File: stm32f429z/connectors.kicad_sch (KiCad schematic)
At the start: 18 parts, among them J1 ADC connector 2, J10 UART 1 connectors, J12 USB to UART GPIO, J14 I2C 1 connector, J2 ADC connector 1, J3 SPI 2 connector, J4 SPI 1 connector, J5 I2C 2 connector, J8 SWD

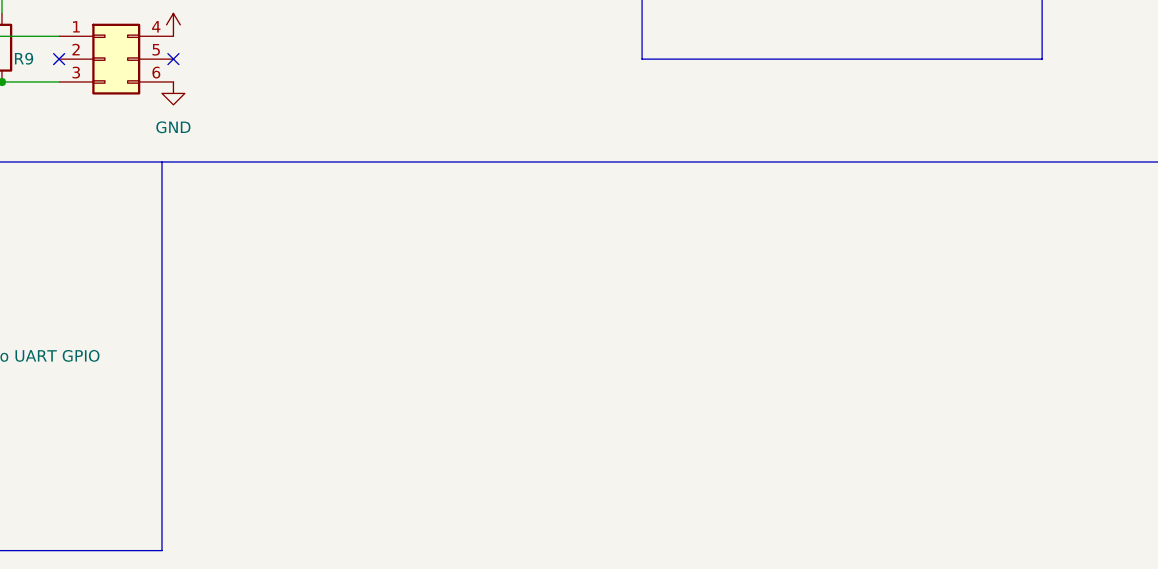
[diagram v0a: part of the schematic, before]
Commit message: removed alot of the silk screen, changed oscillator foor print and added GPIOs
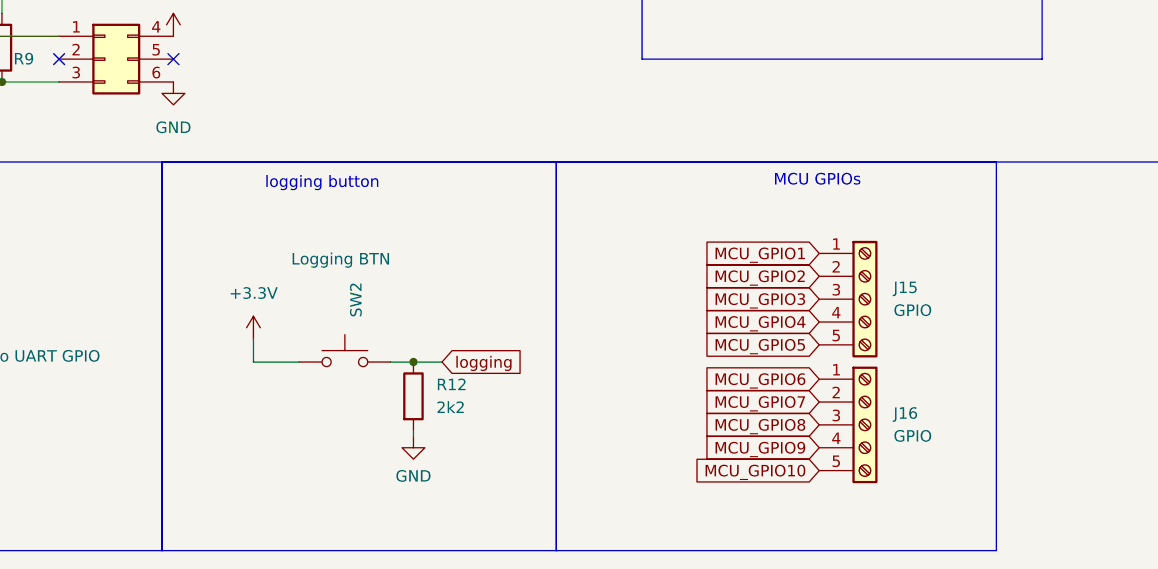
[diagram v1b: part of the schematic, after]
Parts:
- added J15, J16: GPIO, TerminalBlock_Phoenix:TerminalBlock_Phoenix_MKDS-1,5-5_1x05_P5.00mm_Horizontal, symbol Connector:Screw_Terminal_01x05
- added R12: 2k2, Resistor_SMD:R_0603_1608Metric_Pad0.98x0.95mm_HandSolder, symbol Device:R
- added SW2: Logging BTN, Button_Switch_SMD:SW_SPST_PTS645, symbol Switch:SW_Push
- J8: footprint Connector_PinHeader_2.54mm:PinHeader_2x05_P2.54mm_Vertical_SMD -> Connector_PinHeader_2.54mm:PinHeader_2x05_P2.54mm_Vertical
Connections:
- net +3.3V: now also SW2.1
- net GND: now also R12.2
- new net MCU_GPIO1: J15.1 (Pin_1)
- new net MCU_GPIO10: J16.5 (Pin_5)
- new net MCU_GPIO2: J15.2 (Pin_2)
- new net MCU_GPIO3: J15.3 (Pin_3)
- new net MCU_GPIO4: J15.4 (Pin_4)
- new net MCU_GPIO5: J15.5 (Pin_5)
- new net MCU_GPIO6: J16.1 (Pin_1)
- new net MCU_GPIO7: J16.2 (Pin_2)
- new net MCU_GPIO8: J16.3 (Pin_3)
- new net MCU_GPIO9: J16.4 (Pin_4)
- new net logging: R12.1, SW2.2
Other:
- note added: "MCU GPIOs"
- note added: "logging button"

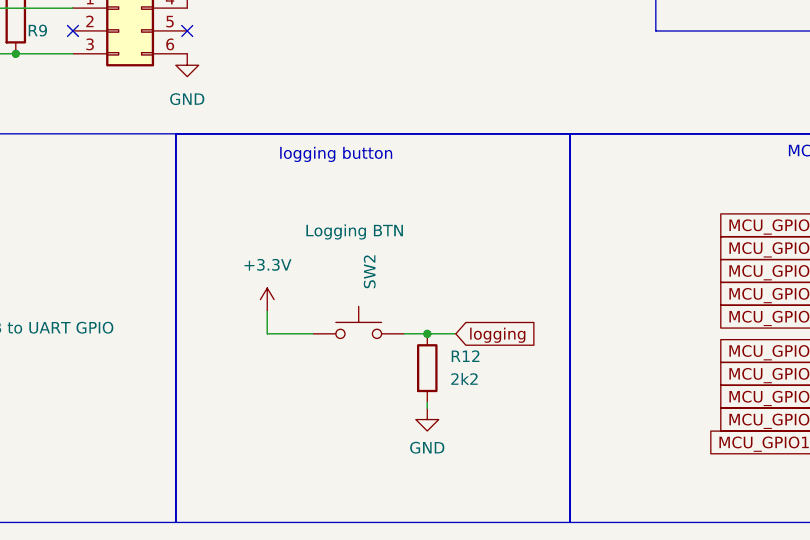
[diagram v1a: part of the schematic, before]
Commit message: changed logging schematic, tweaked some parts of the schematic
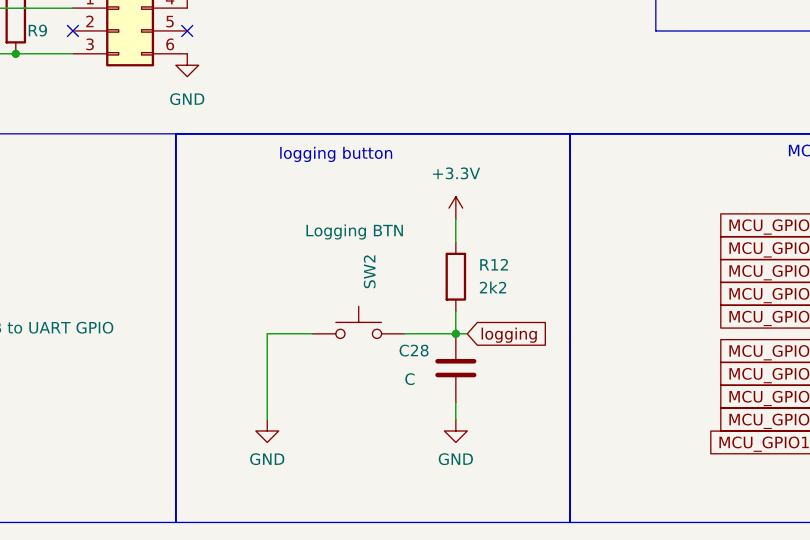
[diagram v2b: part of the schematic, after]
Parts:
- added C28: C, Capacitor_SMD:C_0603_1608Metric_Pad1.08x0.95mm_HandSolder, symbol Device:C
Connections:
- net +3.3V: now also R12.1; no longer SW2.1
- net GND: now also SW2.1, C28.2; no longer R12.2
- net logging: now also R12.2, C28.1; no longer R12.1
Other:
- moved on the sheet: R12
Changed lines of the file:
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@@
   (junction (at 196.85 31.75) (diameter 0) (color 0 0 0 0)
   )
-  (junction (at 177.8 139.065) (diameter 0) (color 0 0 0 0)
-  )
   (junction (at 50.8 88.9) (diameter 0) (color 0 0 0 0)
   )
@@
   )
   (junction (at 203.2 41.91) (diameter 0) (color 0 0 0 0)
+  )
+  (junction (at 180.975 139.065) (diameter 0) (color 0 0 0 0)
   )
   (junction (at 46.99 102.87) (diameter 0) (color 0 0 0 0)
@@
   (no_connect (at 46.99 140.97))
   (no_connect (at 60.96 105.41))
-  (wire (pts (xy 175.26 139.065) (xy 177.8 139.065))
-    (stroke (width 0) (type default))
-  )
   (wire (pts (xy 138.43 107.95) (xy 132.08 107.95))
     (stroke (width 0) (type default))
@@
     (stroke (width 0) (type default))
   )
+  (wire (pts (xy 180.975 148.59) (xy 180.975 146.685))
+    (stroke (width 0) (type default))
+  )
   (wire (pts (xy 196.85 40.64) (xy 196.85 41.91))
     (stroke (width 0) (type default))
@@
     (stroke (width 0) (type default))
   )
+  (wire (pts (xy 160.02 139.065) (xy 160.02 148.59))
+    (stroke (width 0) (type default))
+  )
   (wire (pts (xy 218.44 34.29) (xy 220.98 34.29))
     (stroke (width 0) (type default))
@@
     (stroke (width 0) (type default))
   )
-  (wire (pts (xy 177.8 147.32) (xy 177.8 146.685))
-    (stroke (width 0) (type default))
-  )
   (polyline (pts (xy 187.96 72.39) (xy 284.48 72.39))
     (stroke (width 0) (type default))
@@
     (stroke (width 0) (type default))
   )
-  (wire (pts (xy 177.8 139.065) (xy 180.975 139.065))
+  (wire (pts (xy 175.26 139.065) (xy 180.975 139.065))
     (stroke (width 0) (type default))
   )
@@
     (stroke (width 0) (type default))
   )
+  (wire (pts (xy 180.975 139.065) (xy 182.245 139.065))
+    (stroke (width 0) (type default))
+  )
   (polyline (pts (xy 74.93 24.13) (xy 74.93 72.39))
     (stroke (width 0) (type default))
@@
     (stroke (width 0) (type default))
   )
-  (wire (pts (xy 160.02 139.065) (xy 160.02 136.525))
-    (stroke (width 0) (type default))
-  )
   (wire (pts (xy 132.08 100.33) (xy 132.08 88.9))
     (stroke (width 0) (type default))
@@
     (stroke (width 0) (type default))
   )
+  (wire (pts (xy 180.975 126.365) (xy 180.975 128.905))
+    (stroke (width 0) (type default))
+  )
   (wire (pts (xy 228.6 41.91) (xy 231.14 41.91))
     (stroke (width 0) (type default))
@@
   )
   (wire (pts (xy 60.96 102.87) (xy 46.99 102.87))
+    (stroke (width 0) (type default))
+  )
+  (wire (pts (xy 180.975 136.525) (xy 180.975 139.065))
     (stroke (width 0) (type default))
   )
@@
     )
   )
-  (global_label "logging" (shape input) (at 180.975 139.065 0) (fields_autoplaced)
+  (global_label "logging" (shape input) (at 182.245 139.065 0) (fields_autoplaced)
     (effects (font (size 1.27 1.27)) (justify left))
-    (property "Intersheetrefs" "${INTERSHEET_REFS}" (at 190.9752 139.065 0)
+    (property "Intersheetrefs" "${INTERSHEET_REFS}" (at 192.2452 139.065 0)
       (effects (font (size 1.27 1.27)) (justify left) hide)
     )
@@
     )
   )
-  (symbol (lib_id "Device:R") (at 177.8 142.875 0) (unit 1)
-    (in_bom yes) (on_board yes) (dnp no) (fields_autoplaced)
-    (property "Reference" "R12" (at 180.34 141.605 0)
-      (effects (font (size 1.27 1.27)) (justify left))
-    )
-    (property "Value" "2k2" (at 180.34 144.145 0)
-      (effects (font (size 1.27 1.27)) (justify left))
-    )
-    (property "Footprint" "Resistor_SMD:R_0603_1608Metric_Pad0.98x0.95mm_HandSolder" (at 176.022 142.875 90)
-      (effects (font (size 1.27 1.27)) hide)
-    )
-    (property "Datasheet" "~" (at 177.8 142.875 0)
+  (symbol (lib_id "Device:R") (at 180.975 132.715 0) (unit 1)
+    (in_bom yes) (on_board yes) (dnp no) (fields_autoplaced)
+    (property "Reference" "R12" (at 183.515 131.445 0)
+      (effects (font (size 1.27 1.27)) (justify left))
+    )
+    (property "Value" "2k2" (at 183.515 133.985 0)
+      (effects (font (size 1.27 1.27)) (justify left))
+    )
+    (property "Footprint" "Resistor_SMD:R_0603_1608Metric_Pad0.98x0.95mm_HandSolder" (at 179.197 132.715 90)
+      (effects (font (size 1.27 1.27)) hide)
+    )
+    (property "Datasheet" "~" (at 180.975 132.715 0)
       (effects (font (size 1.27 1.27)) hide)
     )
@@
         (path "/09c21947-d3c4-4f82-9fb4-45f647ba61fc/7392f493-4466-4071-98c2-c2793c4b971d"
           (reference "R12") (unit 1)
+        )
+      )
+    )
+  )
+  (symbol (lib_id "power:GND") (at 180.975 148.59 0) (unit 1)
+    (in_bom yes) (on_board yes) (dnp no) (fields_autoplaced)
+    (property "Reference" "#PWR049" (at 180.975 154.94 0)
+      (effects (font (size 1.27 1.27)) hide)
+    )
+    (property "Value" "GND" (at 180.975 153.035 0)
+      (effects (font (size 1.27 1.27)))
+    )
+    (property "Footprint" "" (at 180.975 148.59 0)
+      (effects (font (size 1.27 1.27)) hide)
+    )
+    (property "Datasheet" "" (at 180.975 148.59 0)
+      (effects (font (size 1.27 1.27)) hide)
+    )
+    (pin "1")
+    (instances
+      (project "stm32f429z"
+        (path "/09c21947-d3c4-4f82-9fb4-45f647ba61fc/7392f493-4466-4071-98c2-c2793c4b971d"
+          (reference "#PWR049") (unit 1)
         )
       )
@@
     )
   )
+  (symbol (lib_id "Device:C") (at 180.975 142.875 0) (unit 1)
+    (in_bom yes) (on_board yes) (dnp no)
+    (property "Reference" "C28" (at 174.625 140.97 0)
+      (effects (font (size 1.27 1.27)) (justify left))
+    )
+    (property "Value" "C" (at 175.26 144.145 0)
+      (effects (font (size 1.27 1.27)) (justify left))
+    )
+    (property "Footprint" "Capacitor_SMD:C_0603_1608Metric_Pad1.08x0.95mm_HandSolder" (at 181.9402 146.685 0)
+      (effects (font (size 1.27 1.27)) hide)
+    )
+    (property "Datasheet" "~" (at 180.975 142.875 0)
+      (effects (font (size 1.27 1.27)) hide)
+    )
+    (pin "1")
+    (pin "2")
+    (instances
+      (project "stm32f429z"
+        (path "/09c21947-d3c4-4f82-9fb4-45f647ba61fc/7392f493-4466-4071-98c2-c2793c4b971d"
+          (reference "C28") (unit 1)
+        )
+      )
+    )
+  )
   (symbol (lib_id "power:+5V") (at 59.69 138.43 0) (unit 1)
     (in_bom yes) (on_board yes) (dnp no) (fields_autoplaced)
@@
     )
   )
-  (symbol (lib_id "power:+3.3V") (at 160.02 136.525 0) (unit 1)
-    (in_bom yes) (on_board yes) (dnp no) (fields_autoplaced)
-    (property "Reference" "#PWR047" (at 160.02 140.335 0)
-      (effects (font (size 1.27 1.27)) hide)
-    )
-    (property "Value" "+3.3V" (at 160.02 131.445 0)
-      (effects (font (size 1.27 1.27)))
-    )
-    (property "Footprint" "" (at 160.02 136.525 0)
-      (effects (font (size 1.27 1.27)) hide)
-    )
-    (property "Datasheet" "" (at 160.02 136.525 0)
-      (effects (font (size 1.27 1.27)) hide)
-    )
-    (pin "1")
-    (instances
-      (project "stm32f429z"
-        (path "/09c21947-d3c4-4f82-9fb4-45f647ba61fc/7392f493-4466-4071-98c2-c2793c4b971d"
-          (reference "#PWR047") (unit 1)
-        )
-      )
-    )
-  )
   (symbol (lib_id "power:+5V") (at 151.13 102.87 0) (unit 1)
     (in_bom yes) (on_board yes) (dnp no) (fields_autoplaced)
@@
     )
   )
-  (symbol (lib_id "power:GND") (at 177.8 147.32 0) (unit 1)
-    (in_bom yes) (on_board yes) (dnp no) (fields_autoplaced)
-    (property "Reference" "#PWR048" (at 177.8 153.67 0)
-      (effects (font (size 1.27 1.27)) hide)
-    )
-    (property "Value" "GND" (at 177.8 151.765 0)
-      (effects (font (size 1.27 1.27)))
-    )
-    (property "Footprint" "" (at 177.8 147.32 0)
-      (effects (font (size 1.27 1.27)) hide)
-    )
-    (property "Datasheet" "" (at 177.8 147.32 0)
+  (symbol (lib_id "power:GND") (at 160.02 148.59 0) (unit 1)
+    (in_bom yes) (on_board yes) (dnp no) (fields_autoplaced)
+    (property "Reference" "#PWR048" (at 160.02 154.94 0)
+      (effects (font (size 1.27 1.27)) hide)
+    )
+    (property "Value" "GND" (at 160.02 153.035 0)
+      (effects (font (size 1.27 1.27)))
+    )
+    (property "Footprint" "" (at 160.02 148.59 0)
+      (effects (font (size 1.27 1.27)) hide)
+    )
+    (property "Datasheet" "" (at 160.02 148.59 0)
       (effects (font (size 1.27 1.27)) hide)
     )
@@
         )
       )
+    )
+  )
+  (symbol (lib_id "power:+3.3V") (at 180.975 126.365 0) (unit 1)
+    (in_bom yes) (on_board yes) (dnp no) (fields_autoplaced)
+    (property "Reference" "#PWR050" (at 180.975 130.175 0)
+      (effects (font (size 1.27 1.27)) hide)
+    )
+    (property "Value" "+3.3V" (at 180.975 121.285 0)
+      (effects (font (size 1.27 1.27)))
+    )
+    (property "Footprint" "" (at 180.975 126.365 0)
+      (effects (font (size 1.27 1.27)) hide)
+    )
+    (property "Datasheet" "" (at 180.975 126.365 0)
+      (effects (font (size 1.27 1.27)) hide)
+    )
+    (pin "1")
+    (instances
+      (project "stm32f429z"
+        (path "/09c21947-d3c4-4f82-9fb4-45f647ba61fc/7392f493-4466-4071-98c2-c2793c4b971d"
+          (reference "#PWR050") (unit 1)
+        )
+      )

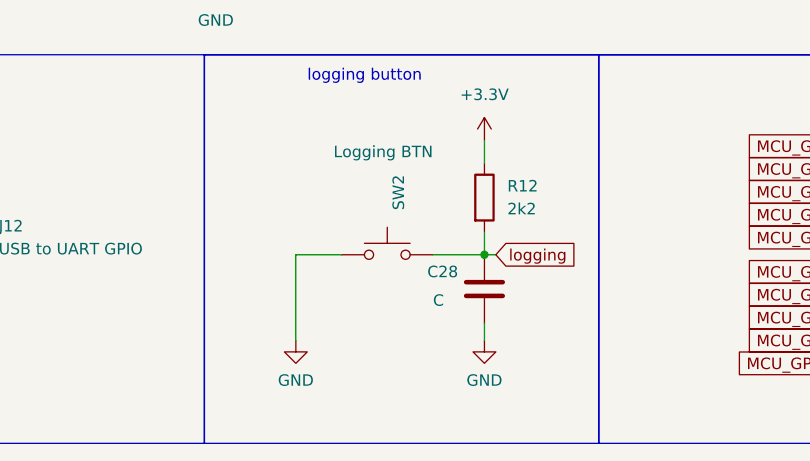
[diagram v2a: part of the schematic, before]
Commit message: changed some footprints, removed dimensions( was causing issues), addd a gerber filter for manufacturing(probably should be regenerated), added a BOM list
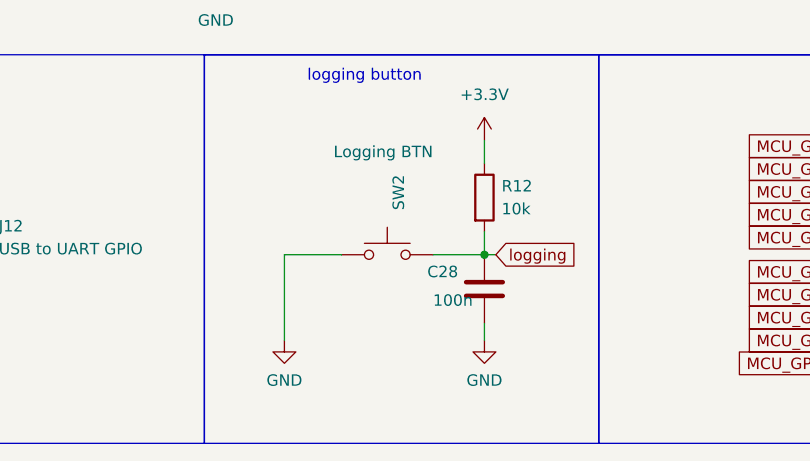
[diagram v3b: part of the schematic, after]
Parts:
- C28: value C -> 100n
- R12: value 2k2 -> 10k
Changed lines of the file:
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@@
     (stroke (width 0) (type default))
   )
-  (wire (pts (xy 160.02 139.065) (xy 160.02 148.59))
+  (wire (pts (xy 158.75 139.065) (xy 158.75 148.59))
     (stroke (width 0) (type default))
   )
@@
     (stroke (width 0) (type default))
   )
-  (wire (pts (xy 165.1 139.065) (xy 160.02 139.065))
-    (stroke (width 0) (type default))
-  )
   (wire (pts (xy 180.975 139.065) (xy 182.245 139.065))
     (stroke (width 0) (type default))
@@
   )
   (wire (pts (xy 128.27 87.63) (xy 128.27 88.9))
+    (stroke (width 0) (type default))
+  )
+  (wire (pts (xy 158.75 139.065) (xy 165.1 139.065))
     (stroke (width 0) (type default))
   )
@@
   (symbol (lib_id "Device:R") (at 180.975 132.715 0) (unit 1)
     (in_bom yes) (on_board yes) (dnp no) (fields_autoplaced)
-    (property "Reference" "R12" (at 183.515 131.445 0)
-      (effects (font (size 1.27 1.27)) (justify left))
-    )
-    (property "Value" "2k2" (at 183.515 133.985 0)
+    (property "Reference" "R12" (at 182.88 131.445 0)
+      (effects (font (size 1.27 1.27)) (justify left))
+    )
+    (property "Value" "10k" (at 182.88 133.985 0)
       (effects (font (size 1.27 1.27)) (justify left))
     )
@@
       (effects (font (size 1.27 1.27)) (justify left))
     )
-    (property "Value" "C" (at 175.26 144.145 0)
+    (property "Value" "100n" (at 175.26 144.145 0)
       (effects (font (size 1.27 1.27)) (justify left))
     )
@@
     )
   )
-  (symbol (lib_id "power:GND") (at 160.02 148.59 0) (unit 1)
-    (in_bom yes) (on_board yes) (dnp no) (fields_autoplaced)
-    (property "Reference" "#PWR048" (at 160.02 154.94 0)
-      (effects (font (size 1.27 1.27)) hide)
-    )
-    (property "Value" "GND" (at 160.02 153.035 0)
-      (effects (font (size 1.27 1.27)))
-    )
-    (property "Footprint" "" (at 160.02 148.59 0)
-      (effects (font (size 1.27 1.27)) hide)
-    )
-    (property "Datasheet" "" (at 160.02 148.59 0)
-      (effects (font (size 1.27 1.27)) hide)
-    )
+  (symbol (lib_id "power:GND") (at 158.75 148.59 0) (unit 1)
+    (in_bom yes) (on_board yes) (dnp no) (fields_autoplaced)
+    (property "Reference" "#PWR048" (at 158.75 154.94 0)
+      (effects (font (size 1.27 1.27)) hide)
+    )
+    (property "Value" "GND" (at 158.75 153.035 0)
+      (effects (font (size 1.27 1.27)))
+    )
+    (property "Footprint" "" (at 158.75 148.59 0)
+      (effects (font (size 1.27 1.27)) hide)
+    )
+    (property "Datasheet" "" (at 158.75 148.59 0)
+      (effects (font (size 1.27 1.27)) hide)
+    )
